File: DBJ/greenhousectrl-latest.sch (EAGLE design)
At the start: 52 parts, among them IC1 ATMEGA168TQFP-08, IC3 7805DT, IC4 L298, J1 5.5x2.1mm Barrel, K1 JQX-15F, Q1 2N3904, Y2 16MHZ

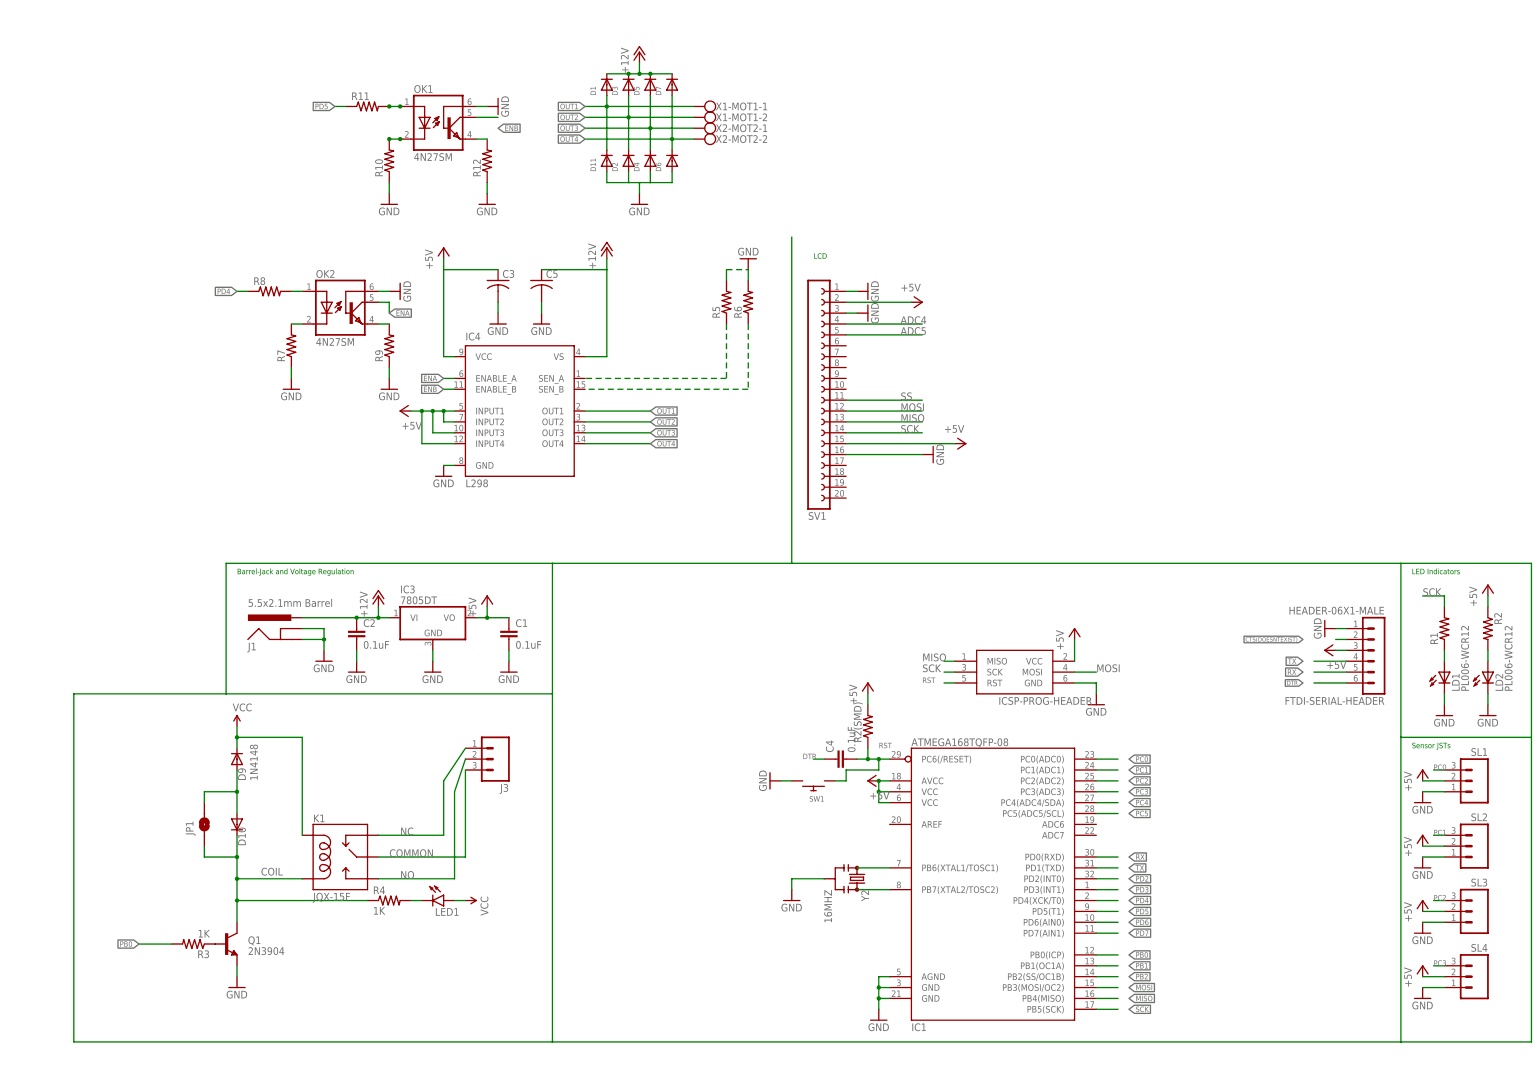
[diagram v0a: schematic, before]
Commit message: Updated Schematic Notes
smaller relay, smd parts added for leds instead of thru-hole, smaller
diodes for h-bridge
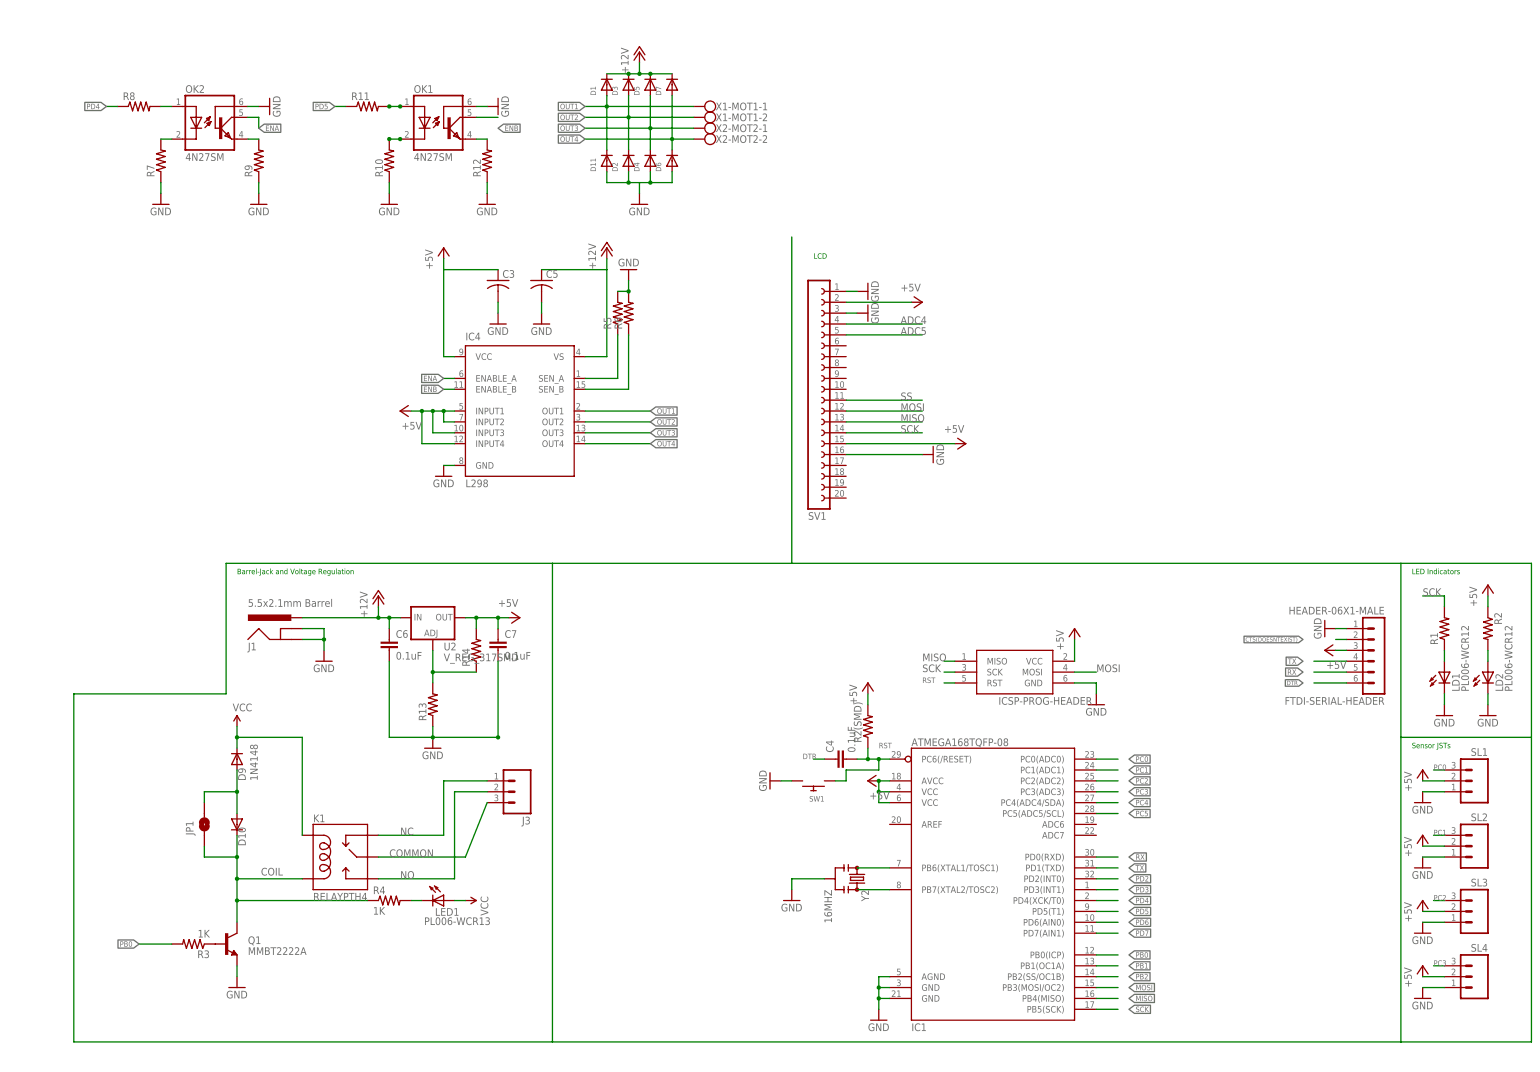
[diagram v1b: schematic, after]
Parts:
- removed C1, C2: 0.1uF, SparkFun-Capacitors:0.1UF-25V(+80/-20%)(0603)
- removed IC3: 7805DT, adafruit:7805DT
- added C6, C7: 0.1uF, SparkFun-Capacitors:0.1UF-25V(+80/-20%)(0603)
- added R13, R14: (no value), SparkFun-Resistors:RESISTOR0402
- added U2: V_REG_317SMD, SparkFun-PowerIC:V_REG_317SMD
- D1, D11, D2, D3, D4, D5, D6, D7: device adafruit:DIODESMA -> adafruit:DIODESOD-523
- K1: value JQX-15F -> RELAYPTH4; device SparkFun-Electromechanical:RELAYPTH5 -> SparkFun-Electromechanical:RELAYPTH4
- LED1: value (none) -> PL006-WCR13; device SparkFun-LED:LED5MM-KIT -> led:PL006-WCR13
- Q1: value 2N3904 -> MMBT2222A; device SparkFun-DiscreteSemi:TRANSISTOR_NPN2N3904-EZ -> SparkFun-DiscreteSemi:TRANSISTOR_NPNMMBT2222A
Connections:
- net N$13 renamed SEN_A
- net N$14 renamed SEN_B
- removed net N$20: D2.A
- new net N$7: R13.2, R14.1, U2.ADJ
- net +12V: now also C6.1, U2.IN; no longer C2.1, IC3.VI
- net +5V: now also C7.1, R14.2, U2.OUT; no longer C1.1, IC3.VO
- net GND: now also C6.2, C7.2, D2.A, R13.1; no longer C1.2, C2.2, IC3.GND
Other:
- moved on the sheet: J3, OK2, R5, R6, R7, R8, R9

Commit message: Updated Schematic
clearly shows subsystems for pcb layout
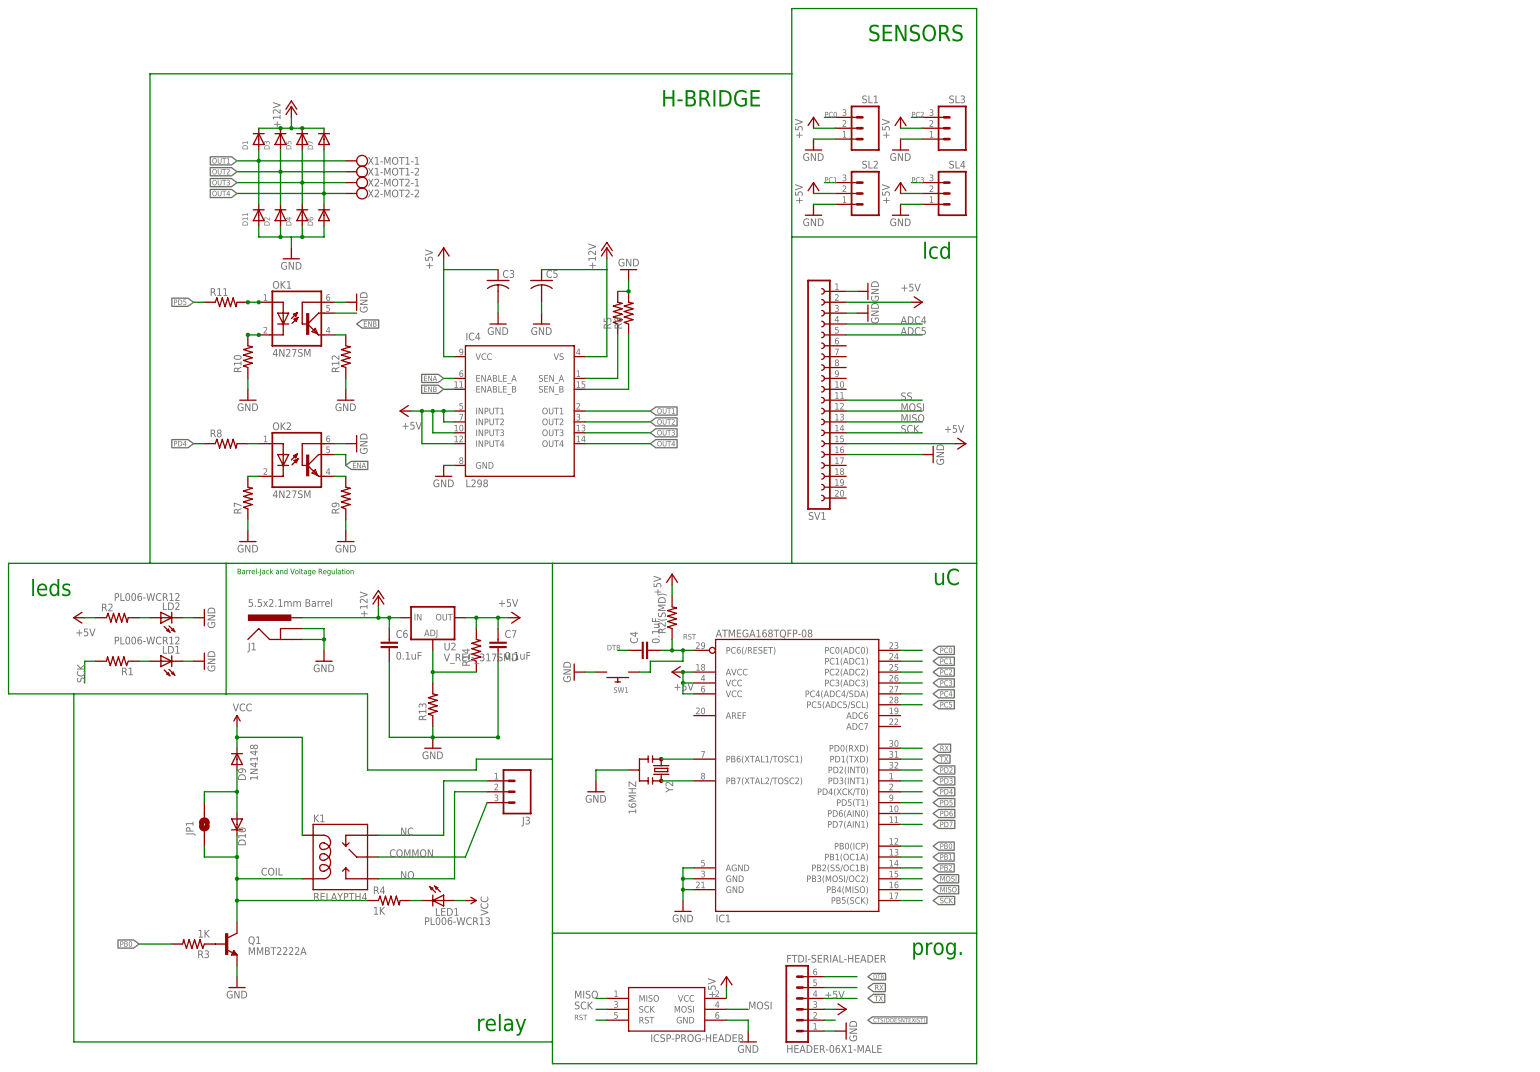
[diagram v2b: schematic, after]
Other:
- note added: "H-BRIDGE"
- note added: "SENSORS"
- note added: "lcd"
- note added: "leds"
- note added: "prog."
- note added: "relay"
- note added: "uC"
- note removed: "LCD"
- note removed: "LED Indicators"
- note removed: "Sensor JSTs"
- moved on the sheet: C4, D1, D11, D2, D3, D4, D5, D6, D7, FTDI-SERIAL-HEADER, IC1, ICSP-PROG-HEADER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
